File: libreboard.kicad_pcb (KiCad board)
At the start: 6 copper layers, 125 x 125 mm, 206 parts, among them J1 USB-C, J10 USB-C, J100 Screw Terminal, J101 Screw Terminal, J11 USB_C_Receptacle_USB2.0, J14 JST_BM04B-SRSS-TB, J15 USB_C_Receptacle, J16 JST_BM04B-SRSS-TB, J17 USB-C, J19 Conn_1x03_Male, J2 Conn_2x07_Male, J22 Conn_HDMI, J3 Conn_1x03_Male, J4 Bus_M.2_Socket_M, J5 Conn_1x22_Female, J51 12V Fan 1, J52 12V Fan 2, J53 12V Fan 3, J54 12V Fan 4, J6 USB-C, J7 Micro_SD_Card_Det, J8 Conn_2x20_Male, SW1 Right angle Tact button, SW2 Right angle Tact button, U1 TPD4EUSB30, U10 EMC2305-x-AP, U11 TUSB4041I, U12 RT9742SNGV, U13 TLV75712PDBVR, U14 TPS552892RYQR, U15 AP22653W6, U16 SN74AHCT1G125DRLR, U17 TCA9538DBR, U18 RT9742GGJ5, U19 TPS3808G01DBVR, U2 TPD4EUSB30, U3 MagJack-A70-112-331N126, U4 TPS552892RYQR, U5 74LVC1G07SE-7, U6 AP22653W6, U7 ASEK-32.768KHZ-L-R-T, U8 AP3441SHE-7B, U9 SK6812, Y1 ECS-2520MV-240-CN-TR

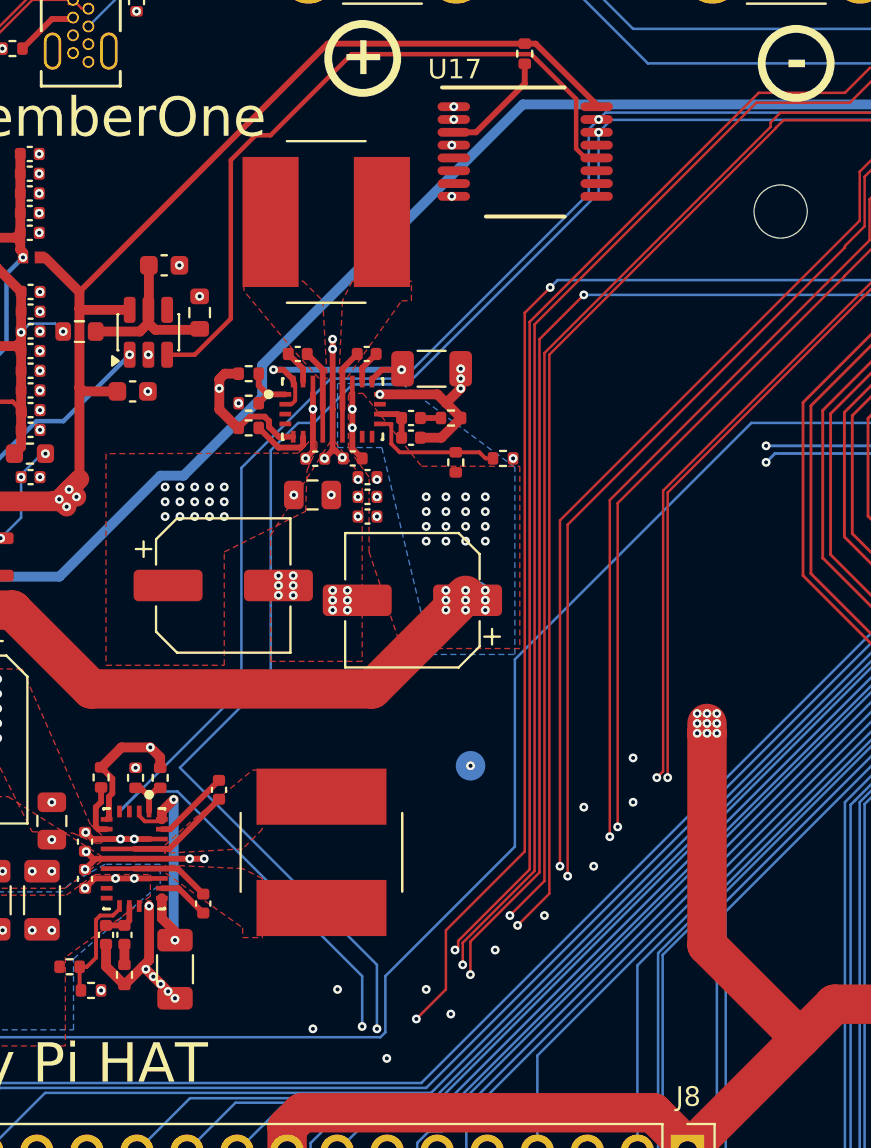
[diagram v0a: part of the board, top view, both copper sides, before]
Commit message: PCB: straighten the ID_SC/ID_SD bus now that U4/U14 are off it
Michael's tidy-up after 479928f: with the regulators no longer on
I2C, the bottom-layer ID_SC/ID_SD run no longer detours past U14 and
U4; VBUS_EN is shifted to make room. Same vias (783).

DRC with schematic parity unchanged: 0 unconnected, no new
violations.

Co-Authored-By: Claude Opus 5.5 <noreply@anthropic.com>
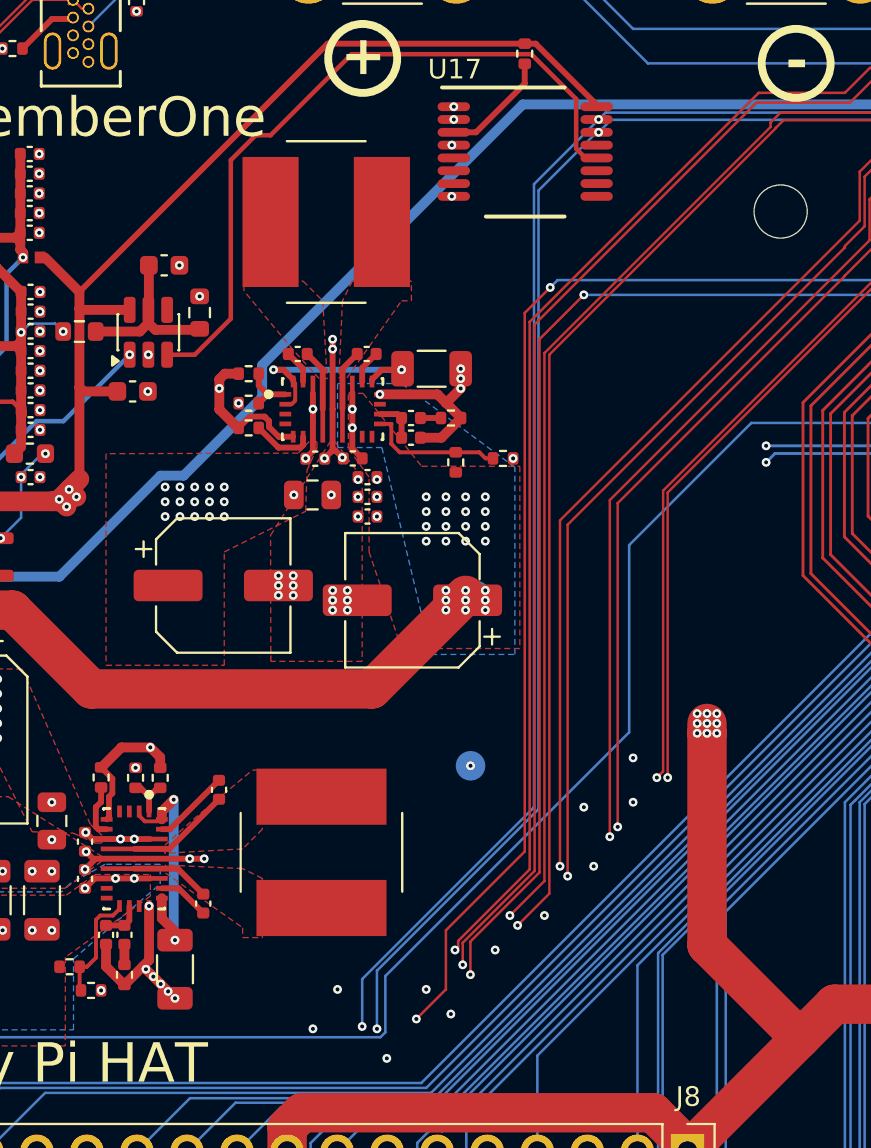
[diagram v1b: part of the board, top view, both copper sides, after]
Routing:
- net /ID_SD: track 262.7 -> 247.2 mm
- net /ID_SC: track 258.2 -> 247.9 mm
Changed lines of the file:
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@@
 	)
 	(segment
-		(start 176.9526 96.304101)
-		(end 176.9526 99.557058)
-		(width 0.13)
-		(layer "B.Cu")
-		(net "/ID_SD")
-	)
-	(segment
-		(start 159.32388 124.734655)
-		(end 153.136544 130.921991)
+		(start 165.4526 139.42883)
+		(end 165.4526 141.834925)
 		(width 0.13)
 		(layer "B.Cu")
@@
 	)
 	(segment
-		(start 165.7026 176.9541)
-		(end 193.4526 176.9541)
+		(start 174.1726 130.70883)
+		(end 165.4526 139.42883)
 		(width 0.13)
 		(layer "B.Cu")
@@
 	)
 	(segment
-		(start 156.083316 129.90749)
-		(end 154.151045 129.90749)
+		(start 174.1726 99.084101)
+		(end 174.1726 130.70883)
 		(width 0.13)
 		(layer "B.Cu")
@@
 	)
 	(segment
-		(start 165.4526 139.276774)
-		(end 156.083316 129.90749)
+		(start 165.7026 176.9541)
+		(end 193.4526 176.9541)
 		(width 0.13)
 		(layer "B.Cu")
@@
 	)
 	(segment
-		(start 165.4526 141.834925)
-		(end 165.4526 139.276774)
-		(width 0.13)
-		(layer "B.Cu")
-		(net "/ID_SD")
-	)
-	(segment
 		(start 165.4526 176.7041)
 		(end 165.7026 176.9541)
@@
 	)
 	(segment
-		(start 163.852602 108.9541)
-		(end 161.552601 111.254101)
-		(width 0.13)
-		(layer "B.Cu")
-		(net "/ID_SD")
-	)
-	(segment
 		(start 177.802601 95.4541)
 		(end 177.4526 95.804101)
@@
 	(segment
 		(start 177.4526 95.804101)
-		(end 176.9526 96.304101)
-		(width 0.13)
-		(layer "B.Cu")
-		(net "/ID_SD")
-	)
-	(segment
-		(start 154.151045 129.90749)
-		(end 153.136544 130.921991)
+		(end 174.1726 99.084101)
 		(width 0.13)
 		(layer "B.Cu")
@@
 	)
 	(segment
-		(start 159.32388 113.482822)
-		(end 159.32388 124.734655)
-		(width 0.13)
-		(layer "B.Cu")
-		(net "/ID_SD")
-	)
-	(segment
-		(start 176.9526 99.557058)
-		(end 167.555558 108.9541)
-		(width 0.13)
-		(layer "B.Cu")
-		(net "/ID_SD")
-	)
-	(segment
 		(start 193.7026 180.7041)
 		(end 193.4526 180.7041)
@@
 	)
 	(segment
-		(start 167.555558 108.9541)
-		(end 163.852602 108.9541)
-		(width 0.13)
-		(layer "B.Cu")
-		(net "/ID_SD")
-	)
-	(segment
-		(start 161.552601 111.254101)
-		(end 159.32388 113.482822)
-		(width 0.13)
-		(layer "B.Cu")
-		(net "/ID_SD")
-	)
-	(segment
 		(start 222.7026 96.4541)
 		(end 221.7026 95.4541)
@@
 	)
 	(segment
-		(start 193.0721 182.0736)
-		(end 193.0721 182.042763)
+		(start 166.2026 141.9541)
+		(end 166.2026 139.0041)
 		(width 0.13)
 		(layer "B.Cu")
@@
 	)
 	(segment
-		(start 232.081056 106.2041)
-		(end 232.3276 106.450644)
+		(start 193.0721 182.0736)
+		(end 193.0721 182.042763)
 		(width 0.13)
 		(layer "B.Cu")
@@
 	)
 	(segment
-		(start 162.2026 111.2041)
-		(end 160.8131 112.5936)
+		(start 232.081056 106.2041)
+		(end 232.3276 106.450644)
 		(width 0.13)
 		(layer "B.Cu")
@@
 	)
 	(segment
-		(start 156.2026 128.7041)
-		(end 166.2026 138.7041)
-		(width 0.13)
-		(layer "B.Cu")
-		(net "/ID_SC")
-	)
-	(segment
-		(start 167.726689 109.253289)
-		(end 164.953411 109.253289)
-		(width 0.13)
-		(layer "B.Cu")
-		(net "/ID_SC")
-	)
-	(segment
-		(start 160.8131 112.5936)
-		(end 160.8131 124.0936)
-		(width 0.13)
-		(layer "B.Cu")
-		(net "/ID_SC")
-	)
-	(segment
-		(start 164.953411 109.253289)
-		(end 163.0026 111.2041)
+		(start 174.4026 99.405645)
+		(end 177.4026 96.405645)
 		(width 0.13)
 		(layer "B.Cu")
@@
 	)
 	(segment
-		(start 166.2026 138.7041)
-		(end 166.2026 141.9541)
+		(start 174.4026 130.8041)
+		(end 174.4026 99.405645)
 		(width 0.13)
 		(layer "B.Cu")
@@
 	)
 	(segment
-		(start 163.0026 111.2041)
-		(end 162.2026 111.2041)
+		(start 166.2026 139.0041)
+		(end 174.4026 130.8041)
 		(width 0.13)
 		(layer "B.Cu")
@@
 	)
 	(segment
-		(start 177.4526 96.4541)
-		(end 177.4526 99.527378)
-		(width 0.13)
-		(layer "B.Cu")
-		(net "/ID_SC")
-	)
-	(segment
-		(start 160.8131 124.0936)
-		(end 156.2026 128.7041)
+		(start 177.4026 96.405645)
+		(end 177.4026 96.4041)
 		(width 0.13)
 		(layer "B.Cu")
@@
 	)
 	(segment
-		(start 177.4526 99.527378)
-		(end 167.726689 109.253289)
+		(start 193.7026 182.2041)
+		(end 193.2026 182.2041)
 		(width 0.13)
 		(layer "B.Cu")
@@
 	)
 	(segment
-		(start 193.7026 182.2041)
-		(end 193.2026 182.2041)
+		(start 177.4026 96.4041)
+		(end 177.4526 96.4541)
 		(width 0.13)
 		(layer "B.Cu")
@@
 	)
 	(segment
-		(start 198.447964 110.9541)
-		(end 197.4526 110.9541)
+		(start 166.6286 142.130555)
+		(end 166.379055 142.3801)
 		(width 0.13)
 		(layer "B.Cu")
@@
 	)
 	(segment
-		(start 199.7026 110.7041)
-		(end 198.697964 110.7041)
+		(start 222.568891 188.9541)
+		(end 222.4526 188.837809)
 		(width 0.13)
 		(layer "B.Cu")
@@
 	)
 	(segment
-		(start 131.3786 142.3801)
-		(end 127.7026 138.7041)
+		(start 166.379055 142.3801)
+		(end 131.3786 142.3801)
 		(width 0.13)
 		(layer "B.Cu")
@@
 	)
 	(segment
-		(start 222.568891 188.9541)
-		(end 222.4526 188.837809)
+		(start 127.7026 122.7041)
+		(end 127.9776 122.4291)
 		(width 0.13)
 		(layer "B.Cu")
@@
 	)
 	(segment
-		(start 166.379055 142.3801)
-		(end 131.3786 142.3801)
+		(start 199.7026 110.7041)
+		(end 198.697964 110.7041)
 		(width 0.13)
 		(layer "B.Cu")
@@
 	)
 	(segment
-		(start 198.697964 110.7041)
-		(end 198.447964 110.9541)
+		(start 127.7026 138.7041)
+		(end 127.7026 122.7041)
 		(width 0.13)
 		(layer "B.Cu")
@@
 	)
 	(segment
-		(start 127.7026 122.7041)
-		(end 127.9776 122.4291)
+		(start 179.0026 117.404099)
+		(end 179.0026 126.9041)
 		(width 0.13)
 		(layer "B.Cu")
@@
 	)
 	(segment
-		(start 166.6286 139.2781)
-		(end 166.6286 142.130555)
+		(start 222.4526 188.837809)
+		(end 222.4526 149.9541)
 		(width 0.13)
 		(layer "B.Cu")
@@
 	)
 	(segment
-		(start 197.4526 110.9541)
-		(end 197.202601 111.204099)
+		(start 127.9776 122.4291)
+		(end 128.8026 122.4291)
 		(width 0.13)
 		(layer "B.Cu")
@@
 	)
 	(segment
-		(start 127.9776 122.4291)
-		(end 128.8026 122.4291)
+		(start 131.3786 142.3801)
+		(end 127.7026 138.7041)
 		(width 0.13)
 		(layer "B.Cu")
@@
 	)
 	(segment
-		(start 197.202601 111.204099)
-		(end 185.2026 111.204099)
+		(start 198.697964 110.7041)
+		(end 198.447964 110.9541)
 		(width 0.13)
 		(layer "B.Cu")
@@
 	)
 	(segment
-		(start 173.2026 132.7041)
-		(end 166.6286 139.2781)
+		(start 197.202601 111.204099)
+		(end 185.2026 111.204099)
 		(width 0.13)
 		(layer "B.Cu")
@@
 	)
 	(segment
-		(start 185.2026 111.204099)
-		(end 173.2026 123.204099)
+		(start 166.6286 139.2781)
+		(end 166.6286 142.130555)
 		(width 0.13)
 		(layer "B.Cu")
@@
 	)
 	(segment
-		(start 166.6286 142.130555)
-		(end 166.379055 142.3801)
+		(start 197.4526 110.9541)
+		(end 197.202601 111.204099)
 		(width 0.13)
 		(layer "B.Cu")
@@
 	)
 	(segment
-		(start 127.7026 138.7041)
-		(end 127.7026 122.7041)
+		(start 179.0026 126.9041)
+		(end 166.6286 139.2781)
 		(width 0.13)
 		(layer "B.Cu")
@@
 	)
 	(segment
-		(start 222.4526 188.837809)
-		(end 222.4526 149.9541)
+		(start 222.4526 149.9541)
+		(end 209.2026 136.7041)
 		(width 0.13)
 		(layer "B.Cu")
@@
 	)
 	(segment
-		(start 222.4526 149.9541)
-		(end 209.2026 136.7041)
+		(start 198.447964 110.9541)
+		(end 197.4526 110.9541)
 		(width 0.13)
 		(layer "B.Cu")
@@
 	)
 	(segment
-		(start 173.2026 123.204099)
-		(end 173.2026 132.7041)
+		(start 185.2026 111.204099)
+		(end 179.0026 117.404099)
 		(width 0.13)
 		(layer "B.Cu")
